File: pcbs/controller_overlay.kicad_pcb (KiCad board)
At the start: 2 copper layers, 19.2 x 58.5 mm, 2 parts

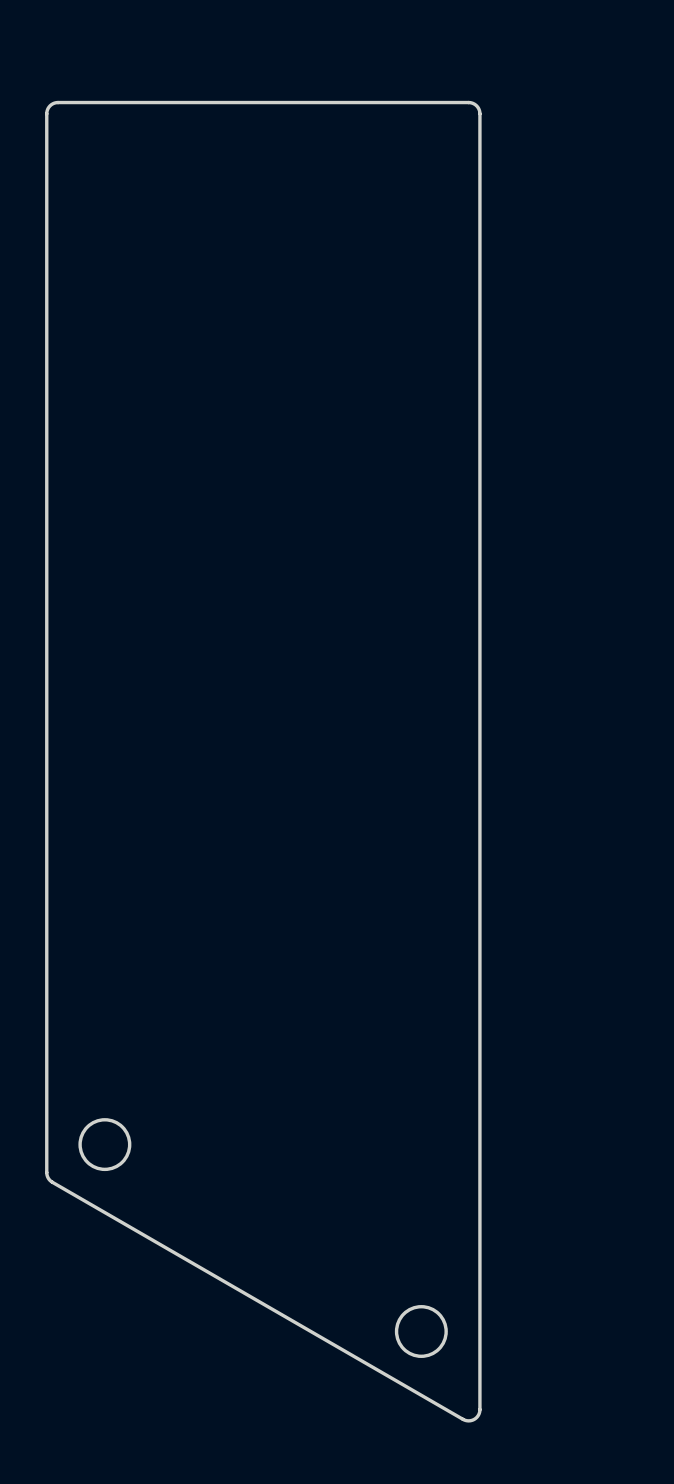
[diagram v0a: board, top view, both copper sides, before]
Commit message: fix(pcb): increase key spacing and correct power switch
Set the PG1316S key pitch to 19.5 mm in both axes and regenerate the tracked PCB and outline artifacts.

Keep the power switch mapping consistent with the intended on/off orientation while preserving the original board outline.
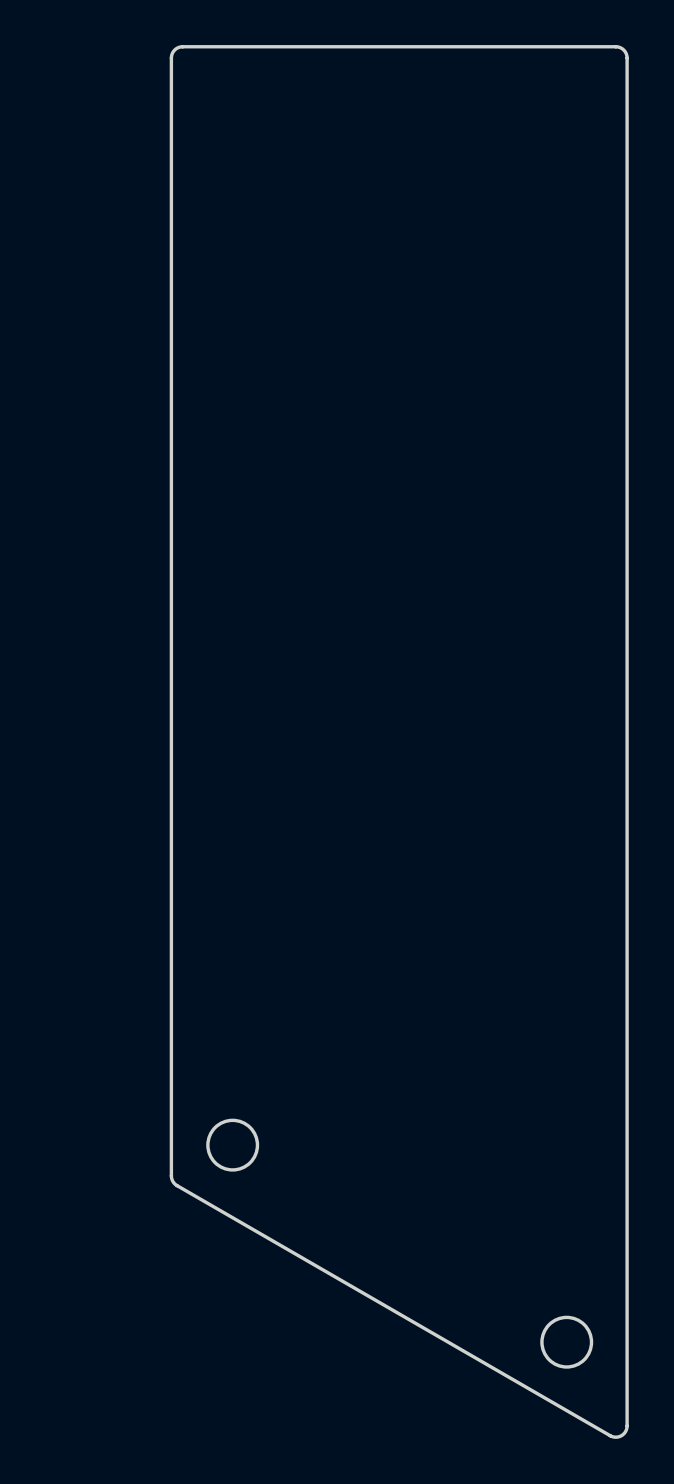
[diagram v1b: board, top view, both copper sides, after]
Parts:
- moved MH2 6.47 mm to (225.4, 109.2)
- moved MH1 5.67 mm to (210.6, 100.5)
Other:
- board size 19.2 x 58.5 mm -> 20.2 x 61.7 mm

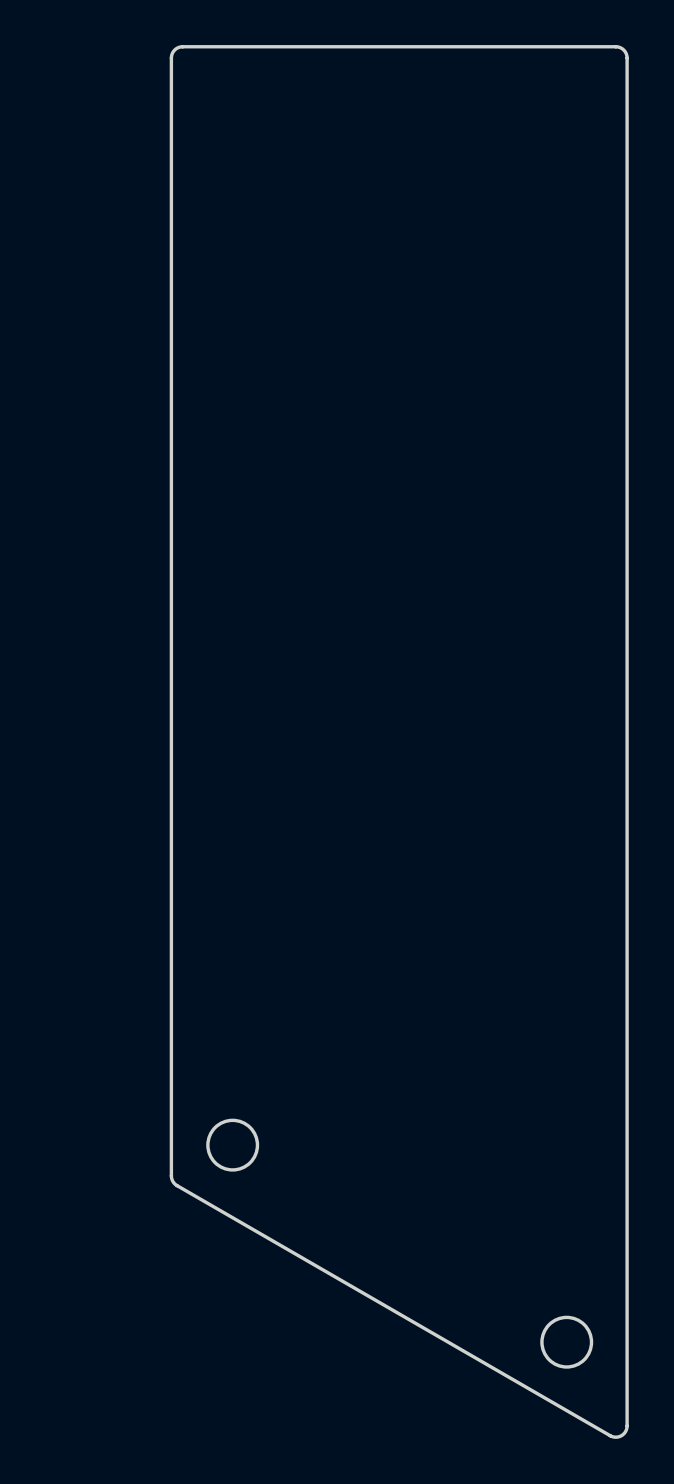
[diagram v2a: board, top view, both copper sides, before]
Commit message: feat: default to compact 18.5 mm layout and refresh generated boards
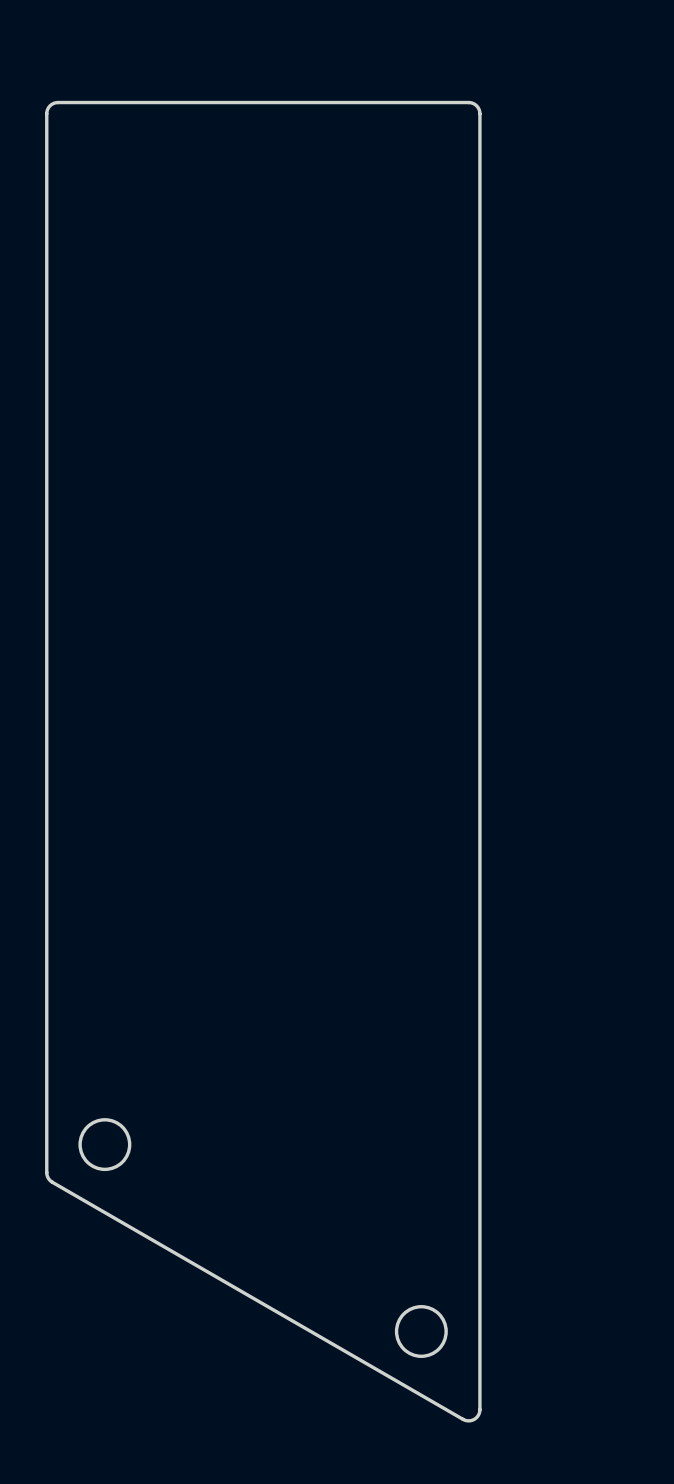
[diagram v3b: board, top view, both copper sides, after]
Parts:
- moved MH2 6.47 mm to (219.0, 108.8)
- moved MH1 5.67 mm to (204.9, 100.5)
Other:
- board size 20.2 x 61.7 mm -> 19.2 x 58.5 mm
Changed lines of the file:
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@@
   (title_block
     (title "controller_overlay")
-    (date "2026-10-17")
+    (date "2026-10-18")
     (rev "0.2")
     (company "ceoloide")
@@
   (footprint "ceoloide:mounting_hole_npth"
     (layer "F.Cu")
-    (at 210.597 100.4885 0)
+    (at 204.927 100.4635 0)
     (property "Reference" "MH1"
       (at 0 2.55 0)
@@
   (footprint "ceoloide:mounting_hole_npth"
     (layer "F.Cu")
-    (at 225.419 109.2325 0)
+    (at 218.969 108.7575 0)
     (property "Reference" "MH2"
       (at 0 2.55 0)
@@
     )
   )
-  (gr_line (start 207.878 101.85080242449034) (end 207.878 52.2525) (layer Edge.Cuts) (stroke (width 0.15) (type default)))
-(gr_line (start 208.378 51.7525) (end 227.59799999999998 51.7525) (layer Edge.Cuts) (stroke (width 0.15) (type default)))
-(gr_line (start 228.09799999999998 52.2525) (end 228.09799999999998 112.94747459811555) (layer Edge.Cuts) (stroke (width 0.15) (type default)))
-(gr_line (start 227.34799999999998 113.38048729811558) (end 208.12800000000001 102.28381512449035) (layer Edge.Cuts) (stroke (width 0.15) (type default)))
-(gr_arc (start 208.378 51.7525) (mid 208.02444659999998 51.898946599999995) (end 207.878 52.2525) (layer Edge.Cuts) (stroke (width 0.15) (type default)))
-(gr_arc (start 228.09799999999998 52.2525) (mid 227.9515534 51.898946599999995) (end 227.59799999999998 51.7525) (layer Edge.Cuts) (stroke (width 0.15) (type default)))
-(gr_arc (start 227.34799999999998 113.38048729811555) (mid 227.84799999999998 113.38048729811555) (end 228.09799999999998 112.94747459811555) (layer Edge.Cuts) (stroke (width 0.15) (type default)))
-(gr_arc (start 207.878 101.85080242449034) (mid 207.94498729999998 102.10080242449034) (end 208.128 102.28381512449035) (layer Edge.Cuts) (stroke (width 0.15) (type default)))
-(gr_circle (center 210.597 100.4885) (end 211.697 100.4885) (layer Edge.Cuts) (stroke (width 0.15) (type default)) (fill none))
-(gr_circle (center 225.419 109.2325) (end 226.519 109.2325) (layer Edge.Cuts) (stroke (width 0.15) (type default)) (fill none))
+  (gr_line (start 202.348 101.70315269366958) (end 202.348 54.7275) (layer Edge.Cuts) (stroke (width 0.15) (type default)))
+(gr_line (start 202.848 54.2275) (end 221.068 54.2275) (layer Edge.Cuts) (stroke (width 0.15) (type default)))
+(gr_line (start 221.568 54.7275) (end 221.568 112.22247459811555) (layer Edge.Cuts) (stroke (width 0.15) (type default)))
+(gr_line (start 220.81799999999998 112.65548729811555) (end 202.598 102.13616539366959) (layer Edge.Cuts) (stroke (width 0.15) (type default)))
+(gr_arc (start 202.848 54.2275) (mid 202.4944466 54.3739466) (end 202.348 54.7275) (layer Edge.Cuts) (stroke (width 0.15) (type default)))
+(gr_arc (start 221.568 54.7275) (mid 221.42155340000002 54.3739466) (end 221.068 54.2275) (layer Edge.Cuts) (stroke (width 0.15) (type default)))
+(gr_arc (start 220.818 112.65548729811556) (mid 221.318 112.65548729811556) (end 221.568 112.22247459811555) (layer Edge.Cuts) (stroke (width 0.15) (type default)))
+(gr_arc (start 202.348 101.70315269366958) (mid 202.4149873 101.95315269366958) (end 202.598 102.13616539366959) (layer Edge.Cuts) (stroke (width 0.15) (type default)))
+(gr_circle (center 204.927 100.4635) (end 206.027 100.4635) (layer Edge.Cuts) (stroke (width 0.15) (type default)) (fill none))
+(gr_circle (center 218.969 108.7575) (end 220.069 108.7575) (layer Edge.Cuts) (stroke (width 0.15) (type default)) (fill none))
 )
